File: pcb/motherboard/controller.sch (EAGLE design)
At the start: 98 parts, among them J1 SNG-2MM-HEADER-04-V, J2 DL-1.25MM-HEADER-20, J3 MICRO_SD, J4 SNG-100-HEADER-01-HDR-V, J5 7498011122R, J6 USB_A, J7 DL-1.25MM-HEADER-10, J8 CUI-PJ-013C, J9 SNG-100-HEADER-05-HDR-V, Q1 12MHz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

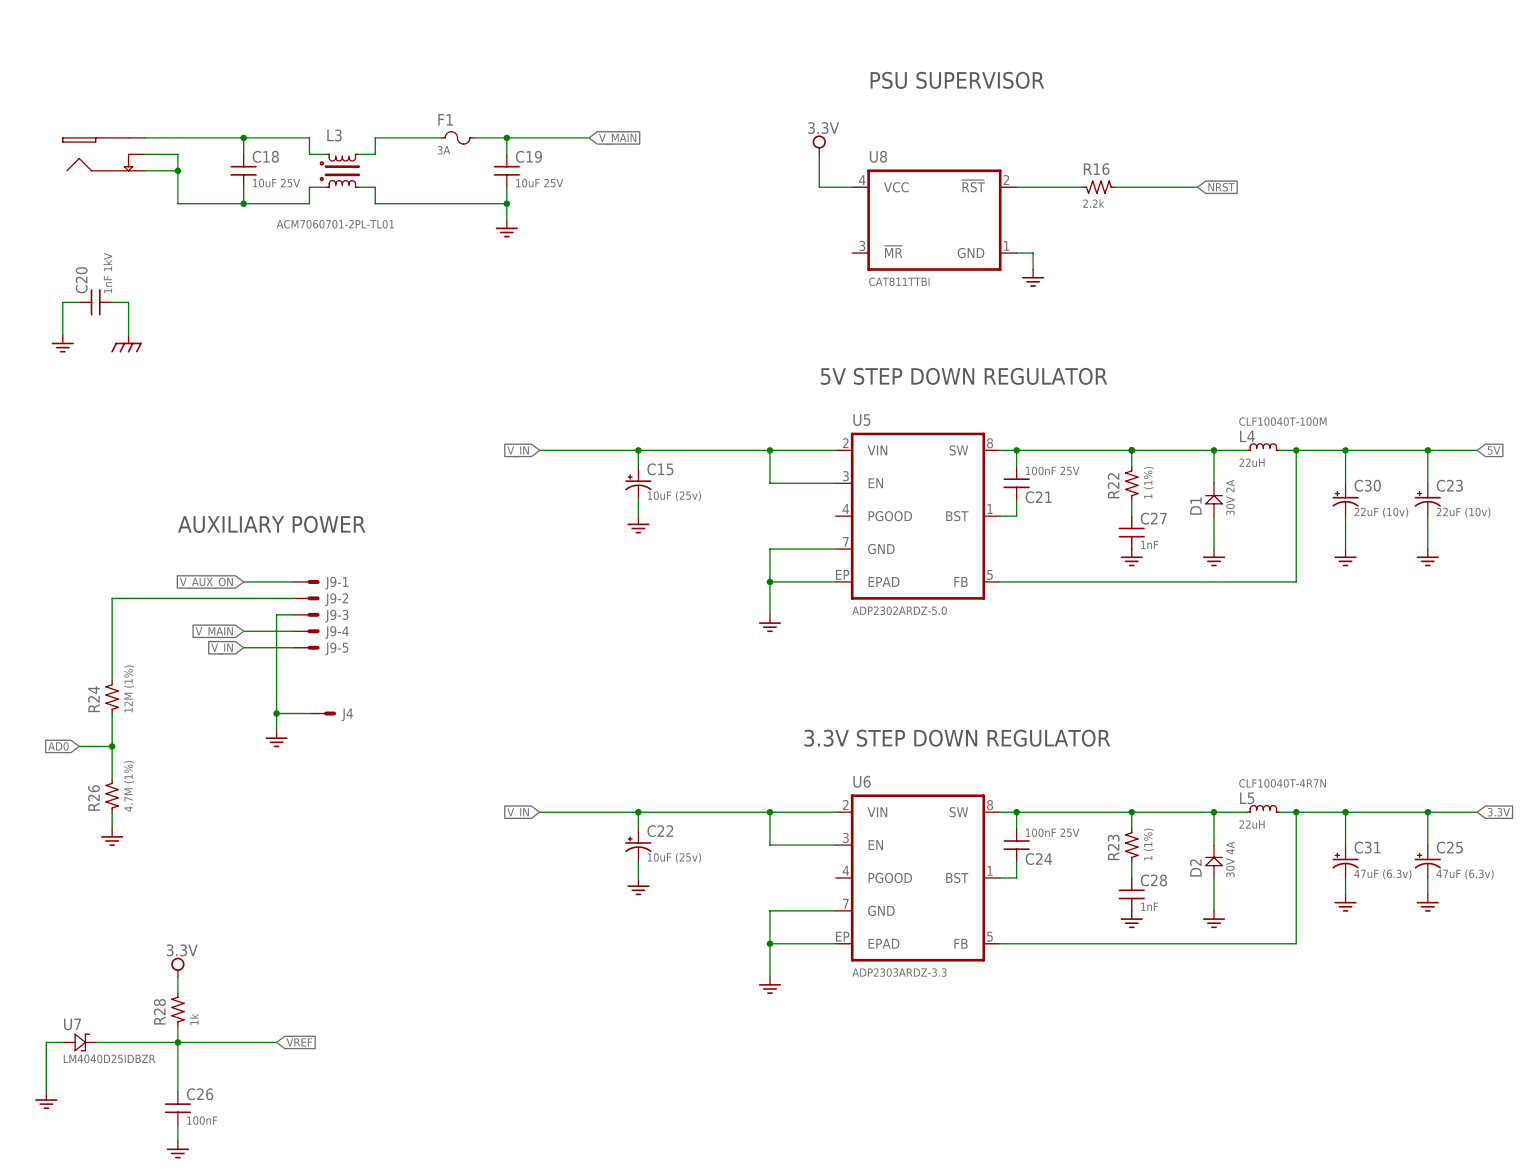
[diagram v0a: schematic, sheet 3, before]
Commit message: Swapped USBC and USBB, USBC will be used for the PCM2704
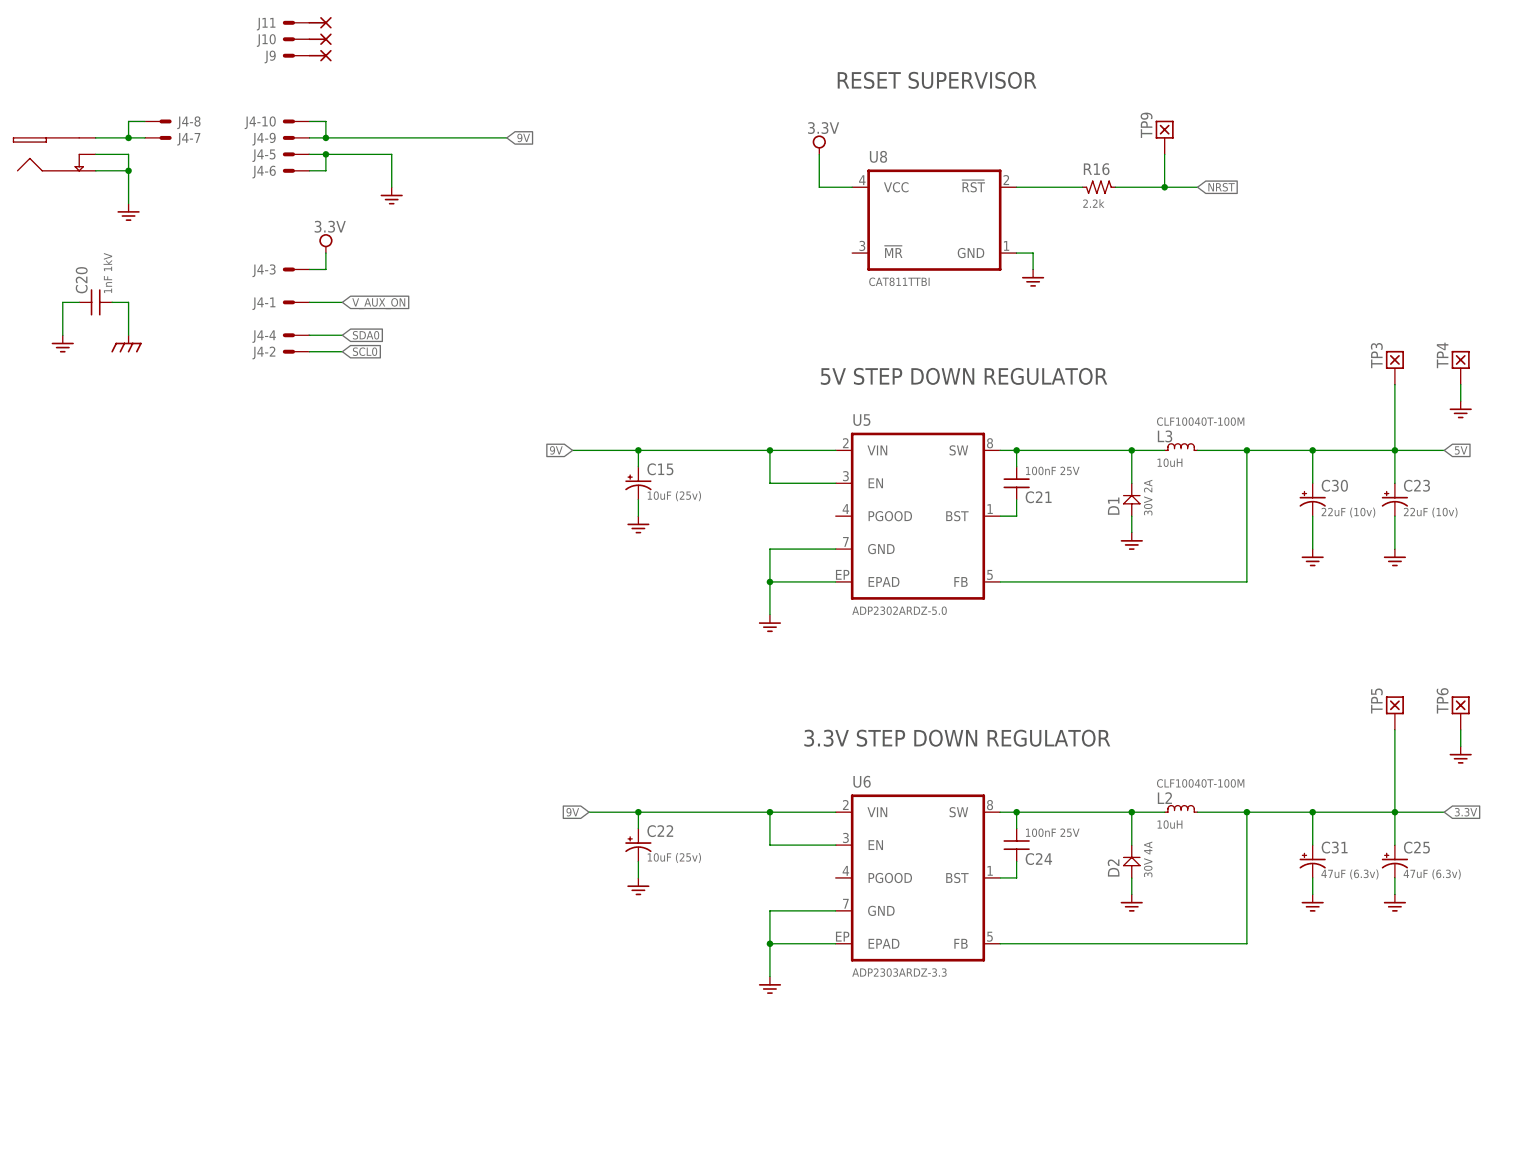
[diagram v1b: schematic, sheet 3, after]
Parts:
- removed C18, C19: 10uF 25V, Passive:CAP-1206
- removed C26: 100nF, Passive:CAP-0603
- removed C27, C28: 1nF, Passive:CAP-0805
- removed F1: 3A, Passive:FUSE1206
- removed L4, L5: 22uH, Passive:IND-10X10
- removed R10, R9: 22, Passive:RES-0603
- removed R11, R12: 15k, Passive:RES-0603
- removed R22, R23: 1 (1%), Passive:RES-0805
- removed R24: 12M (1%), Passive:RES-0603
- removed R26: 4.7M (1%), Passive:RES-0603
- removed R28: 1k, Passive:RES-0603
- removed U7: LM4040D25IDBZR, Passive:TS4040D30IDBZ
- added J10, J11: SNG-100-HEADER-01-HDR-V, Connectors:SNG-100-HEADER-01-HDR-V
- added TP3, TP4, TP5, TP6, TP7, TP8, TP9: (no value), Misc:TEST_POINT-050
- J4: value SNG-100-HEADER-01-HDR-V -> (none); device Connectors:SNG-100-HEADER-01-HDR-V -> Connectors:DL-100-HEADER-10-V; DESCRIPTION (none) -> {DESCRIPTION} Receptacle - Vertical; SKU (none) -> 534206-5
- J9: value SNG-100-HEADER-05-HDR-V -> SNG-100-HEADER-01-HDR-V; device Connectors:SNG-100-HEADER-05-HDR-V -> Connectors:SNG-100-HEADER-01-HDR-V
- L2: value 1A -> 10uH; device Passive:FERRITE -> Passive:IND-10X10; DESCRIPTION {DESCRIPTION} - SMT 0805 - {VALUE} -> (none); PART_NO (none) -> CLF10040T-100M
- L3: value ACM7060701-2PL-TL01 -> 10uH; device Passive:CHOKE-ACM7060701-2PL-TL01 -> Passive:IND-10X10; MFG (none) -> TDK; PART_NO (none) -> CLF10040T-100M
- R17: value (none) -> 0
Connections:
- net N$11 renamed BST_5V
- net N$36 renamed BST_3.3V
- removed net IN_GND: C18.2, J8.GND, J8.SW, L3.IA
- removed net N$2: C27.1, R22.1
- removed net N$3: C28.1, R23.1
- removed net N$32: F1.1, L3.OB
- removed net N$4: C18.1, J8.V+, L3.IB
- removed net N$6: C3.2, DA1.1, J6.GND, L2.2
- removed net N$7: DA1.3, J6.D-, R9.2
- removed net N$8: DA1.2, J6.D+, R10.2
- removed net V_AUX_MON: J9-2.S, R24.2
- removed net V_IN: C15.+, C22.+, J9-5.S, U5.EN, U5.VIN, U6.EN, U6.VIN
- removed net V_MAIN: C19.1, F1.2, J9-4.S
- new net 9V: C15.+, C22.+, J4-10.S, J4-9.S, U5.EN, U5.VIN, U6.EN, U6.VIN
- new net N$23: J4-7.S, J4-8.S, J8.V+
- new net PC20/PWM2: J2-11.S, U2.PC20/PWM2
- net 3.3V: now also J4-3.S, L2.2, TP5.P$1; no longer L5.2, R28.2
- net 5V: now also L3.2, TP3.P$1; no longer L4.2
- net AD0: no longer R24.1, R26.2
- net AD1: no longer J2-11.S
- net DAC_SHDN: now also TP8.P$1
- net EARTH: no longer J6.SHLD@2
- net GND: now also C3.2, DA1.1, J4-5.S, J4-6.S, J6.GND, J8.GND, J8.SW, TP4.P$1, TP6.P$1; no longer C19.2, C26.2, C27.2, C28.2, J4.S, J9-3.S, L2.1, L3.OA, R11.1, R12.1, R26.1, U7.A
- net NRST: now also TP9.P$1
- net SCL0: now also J4-2.S
- net SDA0: now also J4-4.S
- net SW_3.3: now also L2.1; no longer L5.1, R23.2
- net SW_5V: now also L3.1; no longer L4.1, R22.2
- net USBA_D+: now also DA1.2, J6.D+; no longer R10.1, R12.2
- net USBA_D-: now also DA1.3, J6.D-; no longer R11.2, R9.1
- net USBB_D+: now also J1-2.S; no longer R15.1, R2.1
- net USBB_D-: now also J1-3.S; no longer R1.1
- net USBC_D+: now also R15.1, R2.1; no longer J1-3.S
- net USBC_D-: now also R1.1; no longer J1-2.S
- net VOUTL: now also TP7.P$1
- net VREF: no longer C26.1, R28.1, U7.K
- net V_AUX_ON: now also J4-1.S; no longer J9-1.S
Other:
- note added: "EXTERNAL USB PORT"
- note added: "INTERNAL USB PORT (J1)"
- note added: "RESET SUPERVISOR"
- note added: "USB SWITCH"
- note removed: "AUXILIARY POWER"
- note removed: "PSU SUPERVISOR"
- moved on the sheet: C1, C23, C25, C29, C30, C31, D1, D2, J1-1, J1-2, J1-3, J1-4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
